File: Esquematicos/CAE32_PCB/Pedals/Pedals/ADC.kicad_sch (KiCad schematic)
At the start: 2 parts, among them U3 HX711, U5 ADC128S102

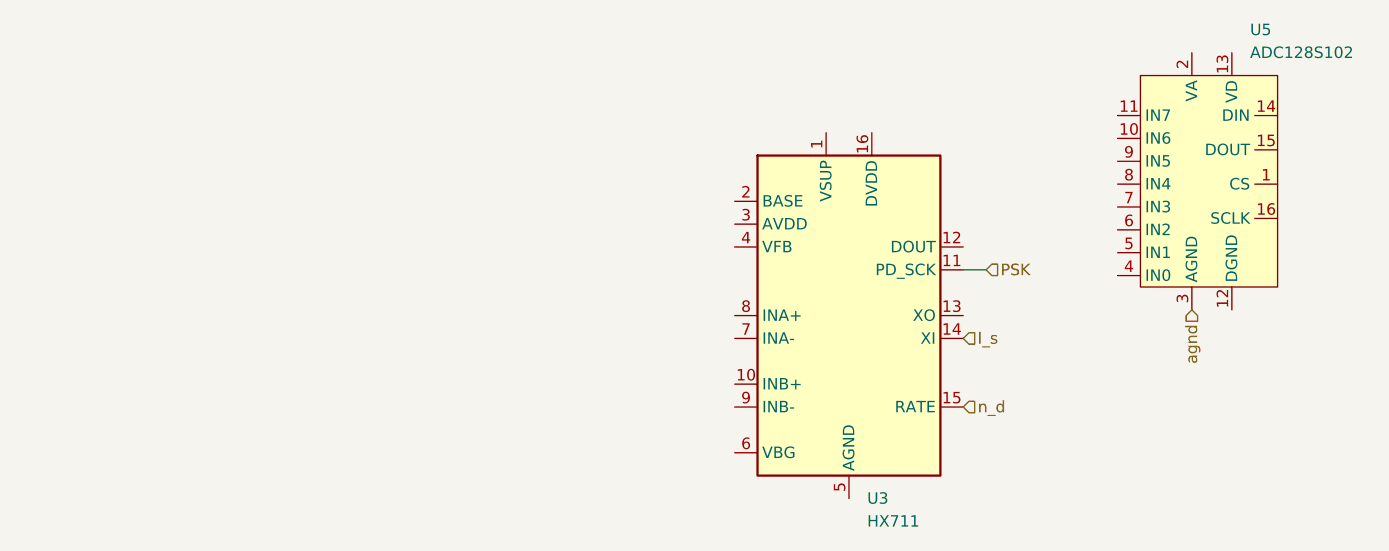
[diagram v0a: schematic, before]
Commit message: chore: se corrigen valores de referencias de componentes, creación de nuevas hojas de diagramas, mejor distribución de componentes
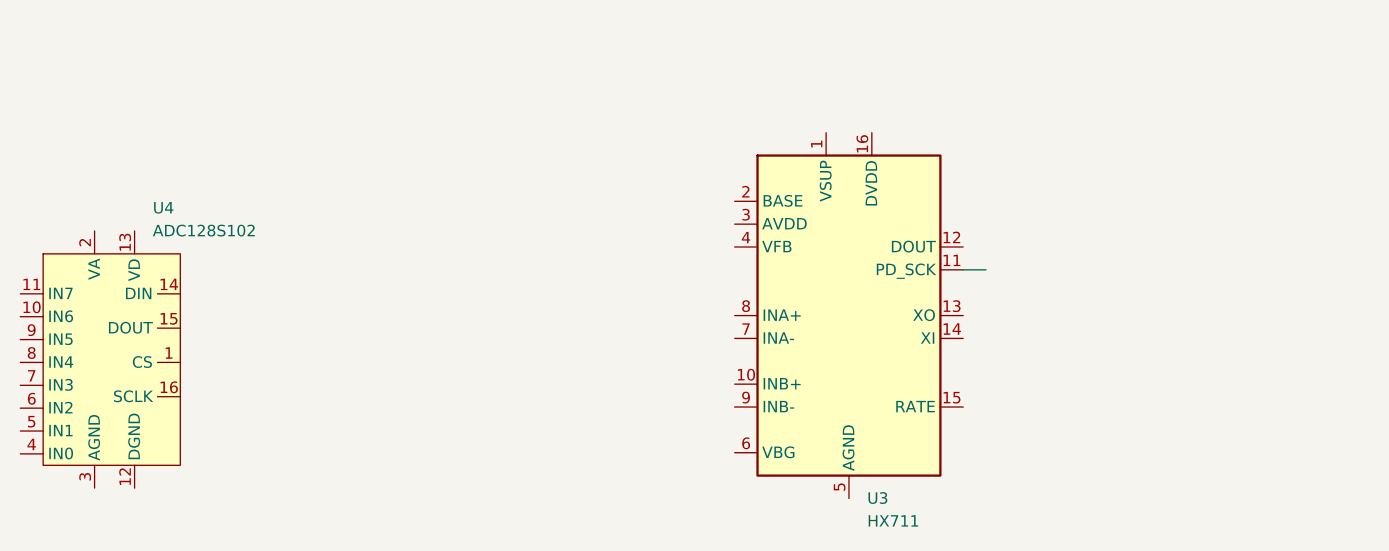
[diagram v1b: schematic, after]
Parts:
- renumbered U5 to U4
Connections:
- net PSK: no longer names the net of U3.11 (PD_SCK)
- net agnd: no longer names the net of U4.3 (AGND)
- net l_s: no longer names the net of U3.14 (XI)
- net n_d: no longer names the net of U3.15 (RATE)
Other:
- company: (none) -> Techtep
- title: (none) -> CAE32 pedals
- moved on the sheet: U4
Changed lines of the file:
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@@
 (kicad_sch (version 20211123) (generator eeschema)
   (paper "A4")
+  (title_block
+    (title "CAE32 pedals")
+    (rev "2")
+    (company "Techtep")
+  )
   (wire (pts (xy 151.765 76.835) (xy 154.305 76.835))
     (stroke (width 0) (type default) (color 0 0 0 0))
-  )
-  (hierarchical_label "n_d" (shape input) (at 151.765 92.075 0)
-    (effects (font (size 1.27 1.27)) (justify left))
-  )
-  (hierarchical_label "l_s" (shape input) (at 151.765 84.455 0)
-    (effects (font (size 1.27 1.27)) (justify left))
-  )
-  (hierarchical_label "agnd" (shape input) (at 177.165 81.28 270)
-    (effects (font (size 1.27 1.27)) (justify right))
-  )
-  (hierarchical_label "PSK" (shape input) (at 154.305 76.835 0)
-    (effects (font (size 1.27 1.27)) (justify left))
   )
   (symbol (lib_id "Analog_ADC:HX711") (at 139.065 81.915 0) (unit 1)
@@
     (pin "9")
   )
-  (symbol (lib_id "Rpizero:ADC128S102") (at 179.07 66.04 0) (unit 1)
+  (symbol (lib_id "Rpizero:ADC128S102") (at 57.15 85.852 0) (unit 1)
     (in_bom yes) (on_board yes) (fields_autoplaced)
-    (property "Reference" "U5" (id 0) (at 183.6294 50.165 0)
+    (property "Reference" "U4" (id 0) (at 61.7094 69.977 0)
       (effects (font (size 1.27 1.27)) (justify left))
     )
-    (property "Value" "ADC128S102" (id 1) (at 183.6294 52.705 0)
+    (property "Value" "ADC128S102" (id 1) (at 61.7094 72.517 0)
       (effects (font (size 1.27 1.27)) (justify left))
     )
-    (property "Footprint" "Package_SO:TSSOP-16_4.4x5mm_P0.65mm" (id 2) (at 179.07 60.96 0)
+    (property "Footprint" "Package_SO:TSSOP-16_4.4x5mm_P0.65mm" (id 2) (at 57.15 80.772 0)
       (effects (font (size 1.27 1.27)) hide)
     )
-    (property "Datasheet" "" (id 3) (at 179.07 60.96 0)
+    (property "Datasheet" "" (id 3) (at 57.15 80.772 0)
       (effects (font (size 1.27 1.27)) hide)
     )

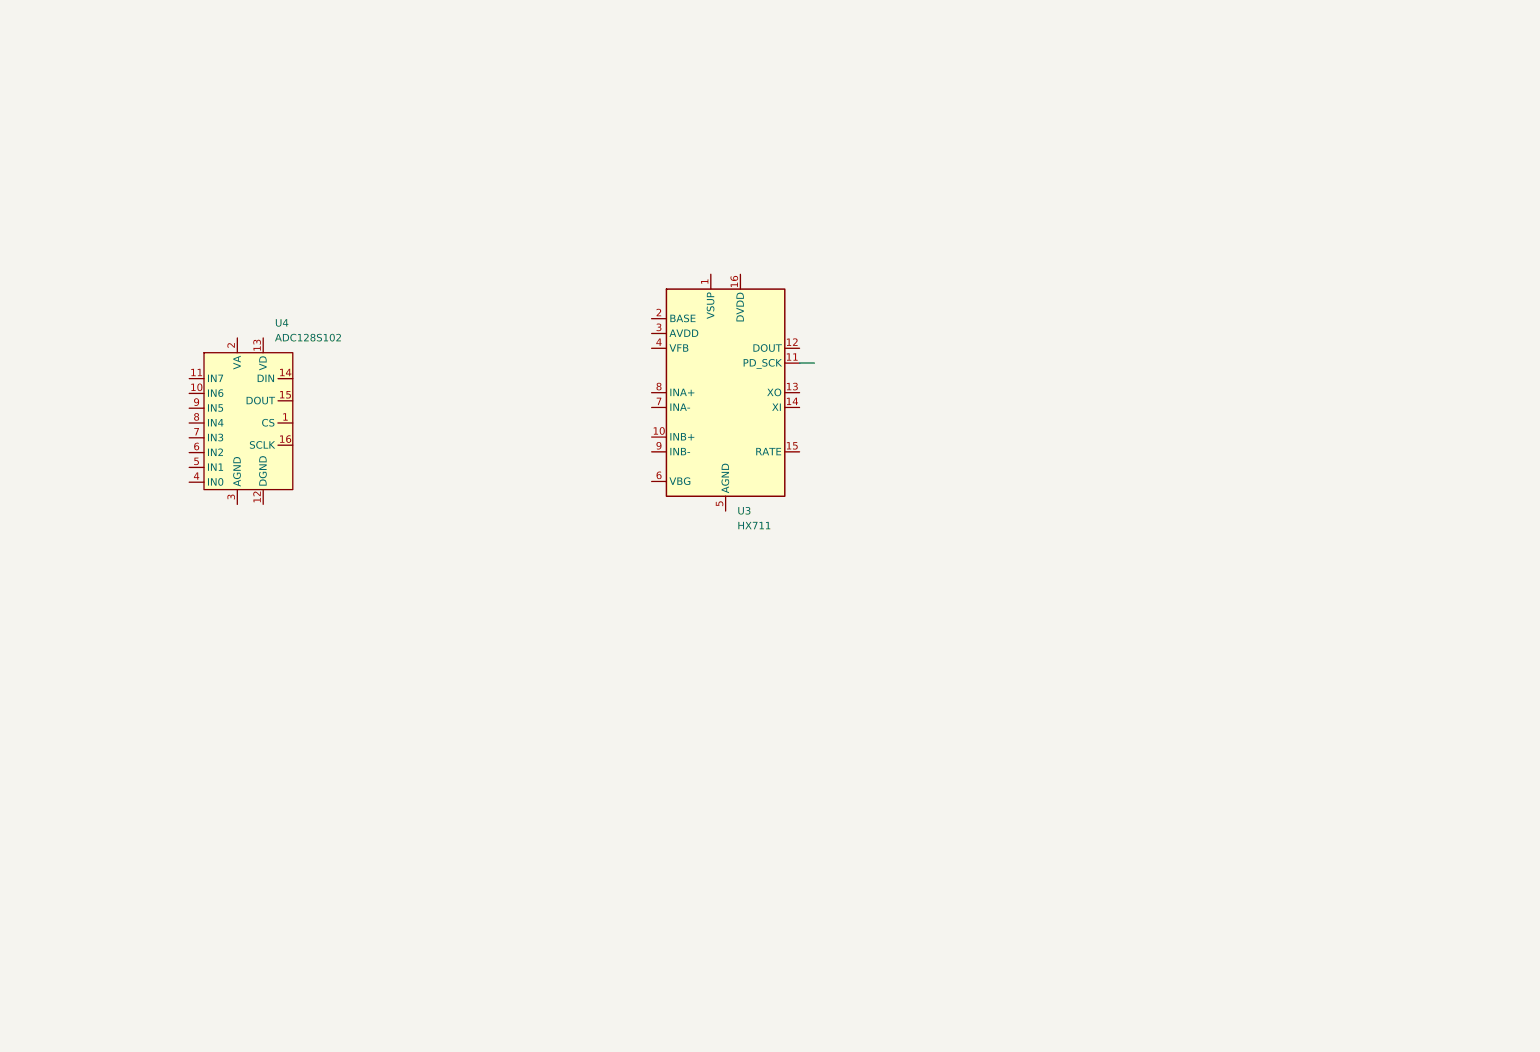
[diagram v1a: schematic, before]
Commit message: update: Primera revision de etapa ADC lista, ademas de una mejor distrubucion de componentes
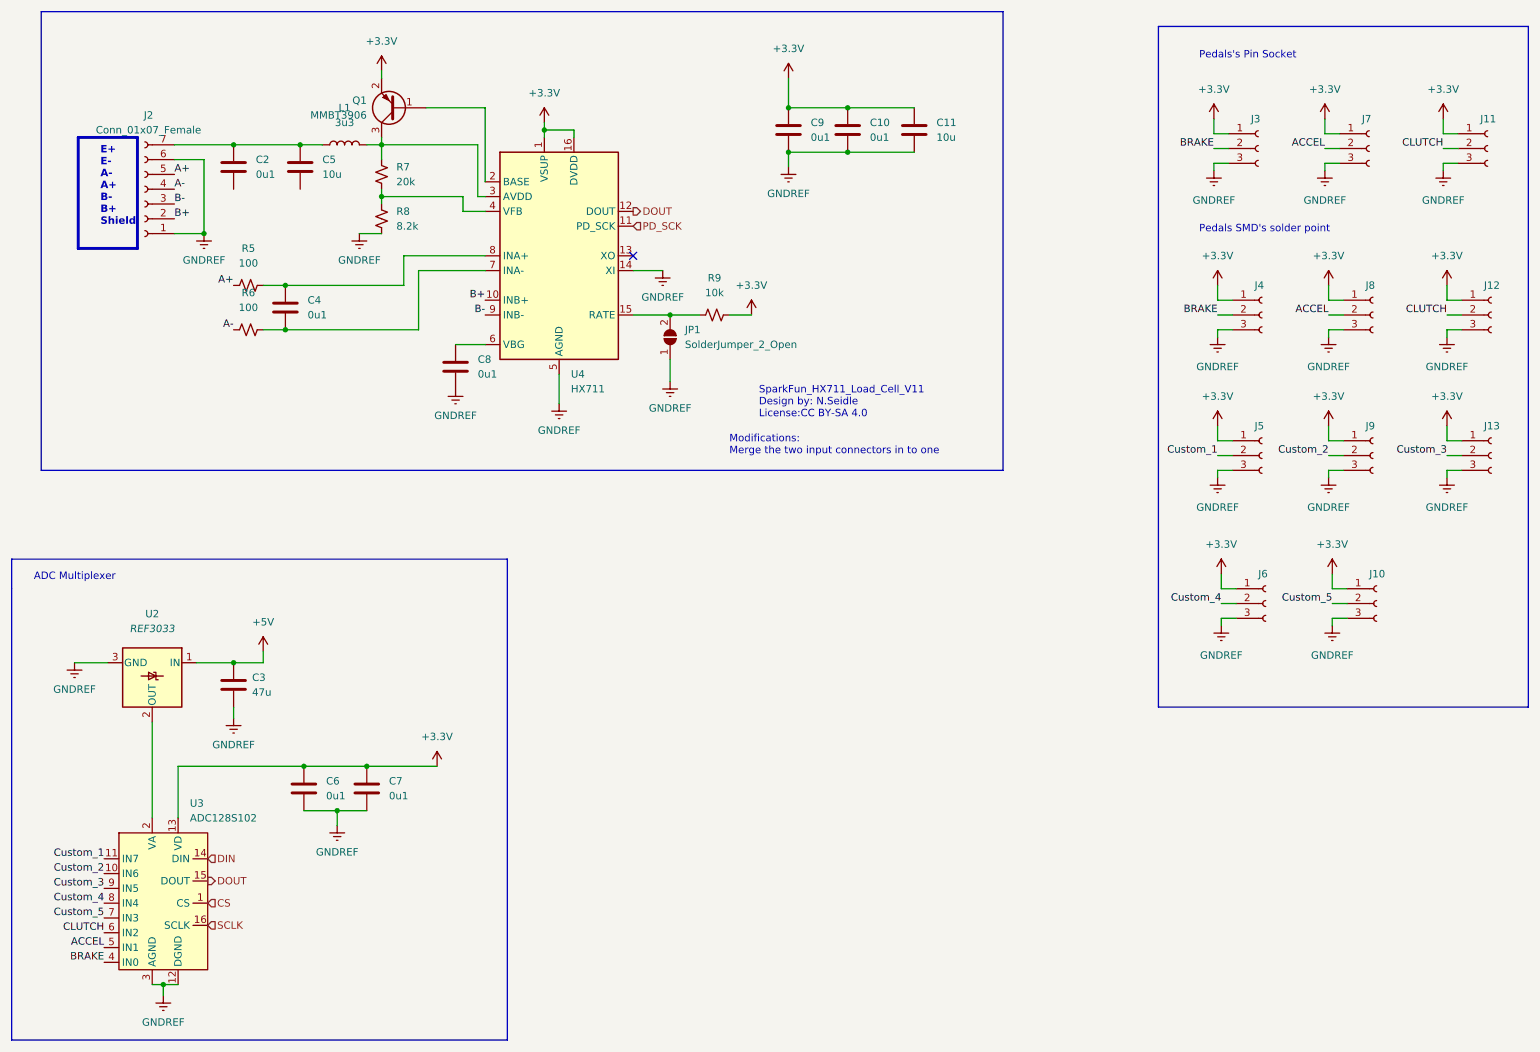
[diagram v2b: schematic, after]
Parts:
- added C10, C2, C4, C6, C7, C8, C9: 0u1, Capacitor_SMD:C_0805_2012Metric_Pad1.18x1.45mm_HandSolder, symbol Device:C
- added C11, C5: 10u, Capacitor_SMD:C_0805_2012Metric_Pad1.18x1.45mm_HandSolder, symbol Device:C
- added C3: 47u, Capacitor_SMD:C_0805_2012Metric_Pad1.18x1.45mm_HandSolder, symbol Device:C
- added J10, J12, J13, J4, J5, J6, J8, J9: Conn_01x03_Female, Extra_components:1x3_pin, symbol Connector:Conn_01x03_Female
- added J11, J3, J7: Conn_01x03_Female, Connector_PinSocket_2.54mm:PinSocket_1x03_P2.54mm_Vertical, symbol Connector:Conn_01x03_Female
- added J2: Conn_01x07_Female, Connector_PinSocket_2.54mm:PinSocket_1x07_P2.54mm_Vertical, symbol Connector:Conn_01x07_Female
- added JP1: SolderJumper_2_Open, Jumper:SolderJumper-2_P1.3mm_Open_RoundedPad1.0x1.5mm, symbol Jumper:SolderJumper_2_Open
- added L1: 3u3, symbol Device:L
- added Q1: MMBT3906, Package_TO_SOT_SMD:SOT-23, symbol Transistor_BJT:MMBT3906
- added R5, R6: 100, Resistor_SMD:R_0805_2012Metric_Pad1.20x1.40mm_HandSolder, symbol Device:R_Small_US
- added R7: 20k, Resistor_SMD:R_0805_2012Metric_Pad1.20x1.40mm_HandSolder, symbol Device:R_Small_US
- added R8: 8.2k, Resistor_SMD:R_0805_2012Metric_Pad1.20x1.40mm_HandSolder, symbol Device:R_Small_US
- added R9: 10k, Resistor_SMD:R_0805_2012Metric_Pad1.20x1.40mm_HandSolder, symbol Device:R_Small_US
- added U2: REF3033, Package_TO_SOT_SMD:SOT-23, symbol Reference_Voltage:REF3033
- renumbered U4 to U3, U3 to U4
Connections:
- net +3.3V: now reaches U4.1 (VSUP)
- net +3.3V: now also U3.13 (VD), U4.16 (DVDD), C10.1, C11.1, C6.1, C7.1, C9.1, J10.1 (Pin_1), J11.1 (Pin_1), J12.1 (Pin_1), J13.1 (Pin_1), J3.1 (Pin_1), J4.1 (Pin_1), J5.1 (Pin_1), J6.1 (Pin_1), J7.1 (Pin_1), J8.1 (Pin_1), J9.1 (Pin_1), Q1.2 (E), R9.2
- net B+: now reaches U4.10 (INB+)
- net B+: now also J2.2 (Pin_2)
- net PD_SCK: now reaches U4.11 (PD_SCK)
- net DOUT: now reaches U4.12 (DOUT)
- net DOUT: now also U3.15 (DOUT)
- net GNDREF: now reaches U4.14 (XI)
- net GNDREF: now also U3.12 (DGND), U3.3 (AGND), U4.5 (AGND), C10.2, C11.2, C3.2, C6.2, C7.2, C8.2, C9.2, J10.3 (Pin_3), J11.3 (Pin_3), J12.3 (Pin_3), J13.3 (Pin_3), J2.1 (Pin_1), J2.6 (Pin_6), J3.3 (Pin_3), J4.3 (Pin_3), J5.3 (Pin_3), J6.3 (Pin_3), J7.3 (Pin_3), J8.3 (Pin_3), J9.3 (Pin_3), JP1.1 (A), R8.2, U2.3 (GND)
- net at U4.15 (RATE): now also JP1.2 (B), R9.1
- net at U4.2 (BASE): now also Q1.1 (B)
- net at U4.3 (AVDD): now also L1.2, Q1.3 (C), R7.1
- net at U4.4 (VFB): now also R7.2, R8.1
- net at U4.6 (VBG): now also C8.1
- net at U4.7 (INA-): now also C4.2, R6.1
- net at U4.8 (INA+): now also C4.1, R5.2
- net B-: now reaches U4.9 (INB-)
- net B-: now also J2.3 (Pin_3)
- net CS: now reaches U3.1 (CS)
- net Custom_2: now reaches U3.10 (IN6)
- net Custom_2: now also J9.2 (Pin_2)
- net Custom_1: now reaches U3.11 (IN7)
- net Custom_1: now also J5.2 (Pin_2)
- net DIN: now reaches U3.14 (DIN)
- net SCLK: now reaches U3.16 (SCLK)
- net at U3.2 (VA): now also U2.2 (OUT)
- net BRAKE: now reaches U3.4 (IN0)
- net BRAKE: now also J3.2 (Pin_2), J4.2 (Pin_2)
- net ACCEL: now reaches U3.5 (IN1)
- net ACCEL: now also J7.2 (Pin_2), J8.2 (Pin_2)
- net CLUTCH: now reaches U3.6 (IN2)
- net CLUTCH: now also J11.2 (Pin_2), J12.2 (Pin_2)
- net Custom_5: now reaches U3.7 (IN3)
- net Custom_5: now also J10.2 (Pin_2)
- net Custom_4: now reaches U3.8 (IN4)
- net Custom_4: now also J6.2 (Pin_2)
- net Custom_3: now reaches U3.9 (IN5)
- net Custom_3: now also J13.2 (Pin_2)
- new net: C2.1, C5.1, J2.7 (Pin_7), L1.1
- new net +5V: C3.1, U2.1 (IN)
- new net A+: J2.5 (Pin_5), R5.1
- new net A-: J2.4 (Pin_4), R6.2
- no-connect marks 0 -> 1
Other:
- note added: "ADC Multiplexer"
- note added: "E+ E- A- A+ B- B+ Shield"
- note added: "Modifications: Merge the two input connectors in to one"
- note added: "Pedals SMD's solder point"
- note added: "Pedals's Pin Socket"
- note added: "SparkFun_HX711_Load_Cell_V11 Design by: N.Seidle License:CC BY-SA 4.0"
- company: Techtep -> (none)
- moved on the sheet: U3, U4

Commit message: update: se añade otra hoja para las celdas de carga, ademas de reorganizar todas las hojas
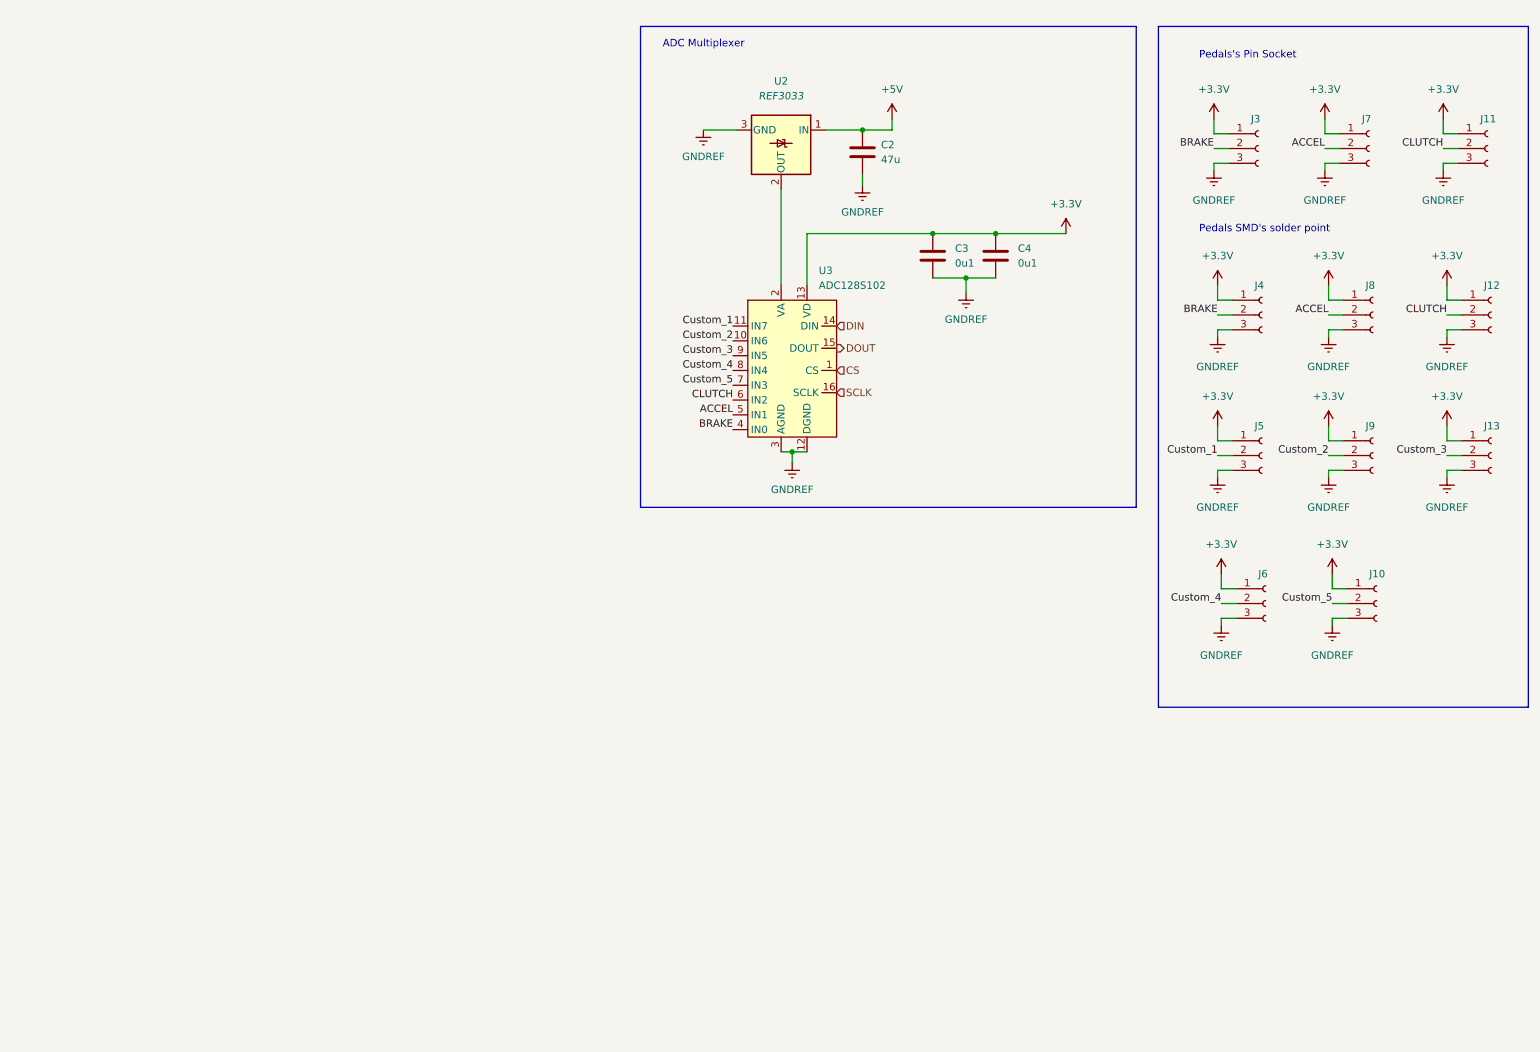
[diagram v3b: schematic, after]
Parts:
- removed C10, C2, C4, C8, C9: 0u1, Capacitor_SMD:C_0805_2012Metric_Pad1.18x1.45mm_HandSolder, symbol Device:C
- removed C11, C5: 10u, Capacitor_SMD:C_0805_2012Metric_Pad1.18x1.45mm_HandSolder, symbol Device:C
- removed J2: Conn_01x07_Female, Connector_PinSocket_2.54mm:PinSocket_1x07_P2.54mm_Vertical, symbol Connector:Conn_01x07_Female
- removed JP1: SolderJumper_2_Open, Jumper:SolderJumper-2_P1.3mm_Open_RoundedPad1.0x1.5mm, symbol Jumper:SolderJumper_2_Open
- removed L1: 3u3, symbol Device:L
- removed Q1: MMBT3906, Package_TO_SOT_SMD:SOT-23, symbol Transistor_BJT:MMBT3906
- removed R5, R6: 100, Resistor_SMD:R_0805_2012Metric_Pad1.20x1.40mm_HandSolder, symbol Device:R_Small_US
- removed R7: 20k, Resistor_SMD:R_0805_2012Metric_Pad1.20x1.40mm_HandSolder, symbol Device:R_Small_US
- removed R8: 8.2k, Resistor_SMD:R_0805_2012Metric_Pad1.20x1.40mm_HandSolder, symbol Device:R_Small_US
- removed R9: 10k, Resistor_SMD:R_0805_2012Metric_Pad1.20x1.40mm_HandSolder, symbol Device:R_Small_US
- removed U4: HX711, Package_SO:SOP-16_3.9x9.9mm_P1.27mm, symbol Analog_ADC:HX711
- C2: renamed from C3; footprint Capacitor_SMD:C_0805_2012Metric_Pad1.18x1.45mm_HandSolder -> Capacitor_SMD:C_0603_1608Metric_Pad1.08x0.95mm_HandSolder
- C3: renamed from C6; footprint Capacitor_SMD:C_0805_2012Metric_Pad1.18x1.45mm_HandSolder -> Capacitor_SMD:C_0603_1608Metric_Pad1.08x0.95mm_HandSolder
- C4: renamed from C7; footprint Capacitor_SMD:C_0805_2012Metric_Pad1.18x1.45mm_HandSolder -> Capacitor_SMD:C_0603_1608Metric_Pad1.08x0.95mm_HandSolder
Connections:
- no-connect marks 1 -> 0
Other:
- note removed: "E+ E- A- A+ B- B+ Shield"
- note removed: "Modifications: Merge the two input connectors in to one"
- note removed: "SparkFun_HX711_Load_Cell_V11 Design by: N.Seidle License:CC BY-SA 4.0"
- moved on the sheet: C2, C3, C4, U2, U3
